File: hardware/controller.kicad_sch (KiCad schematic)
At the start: 2 parts

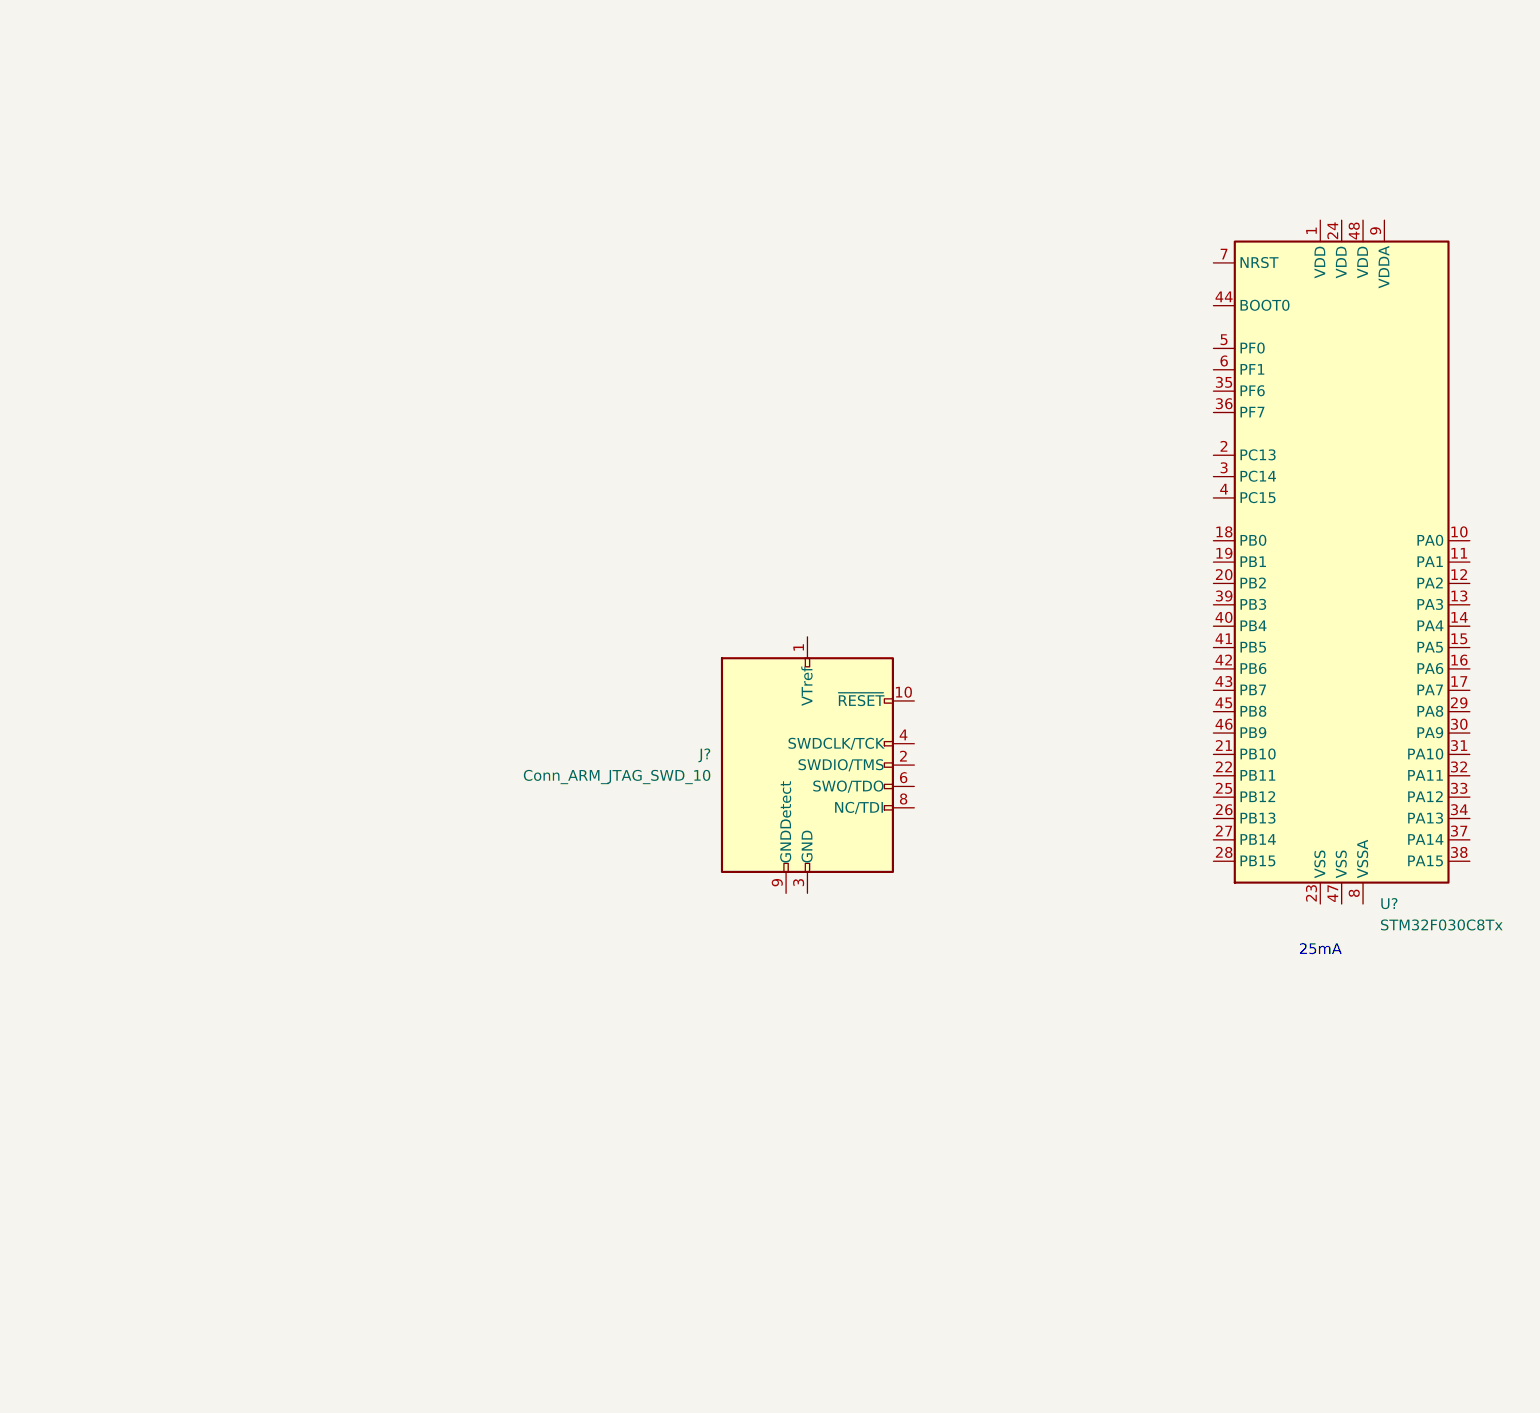
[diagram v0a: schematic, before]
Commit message: MAX5715BAUD lib added
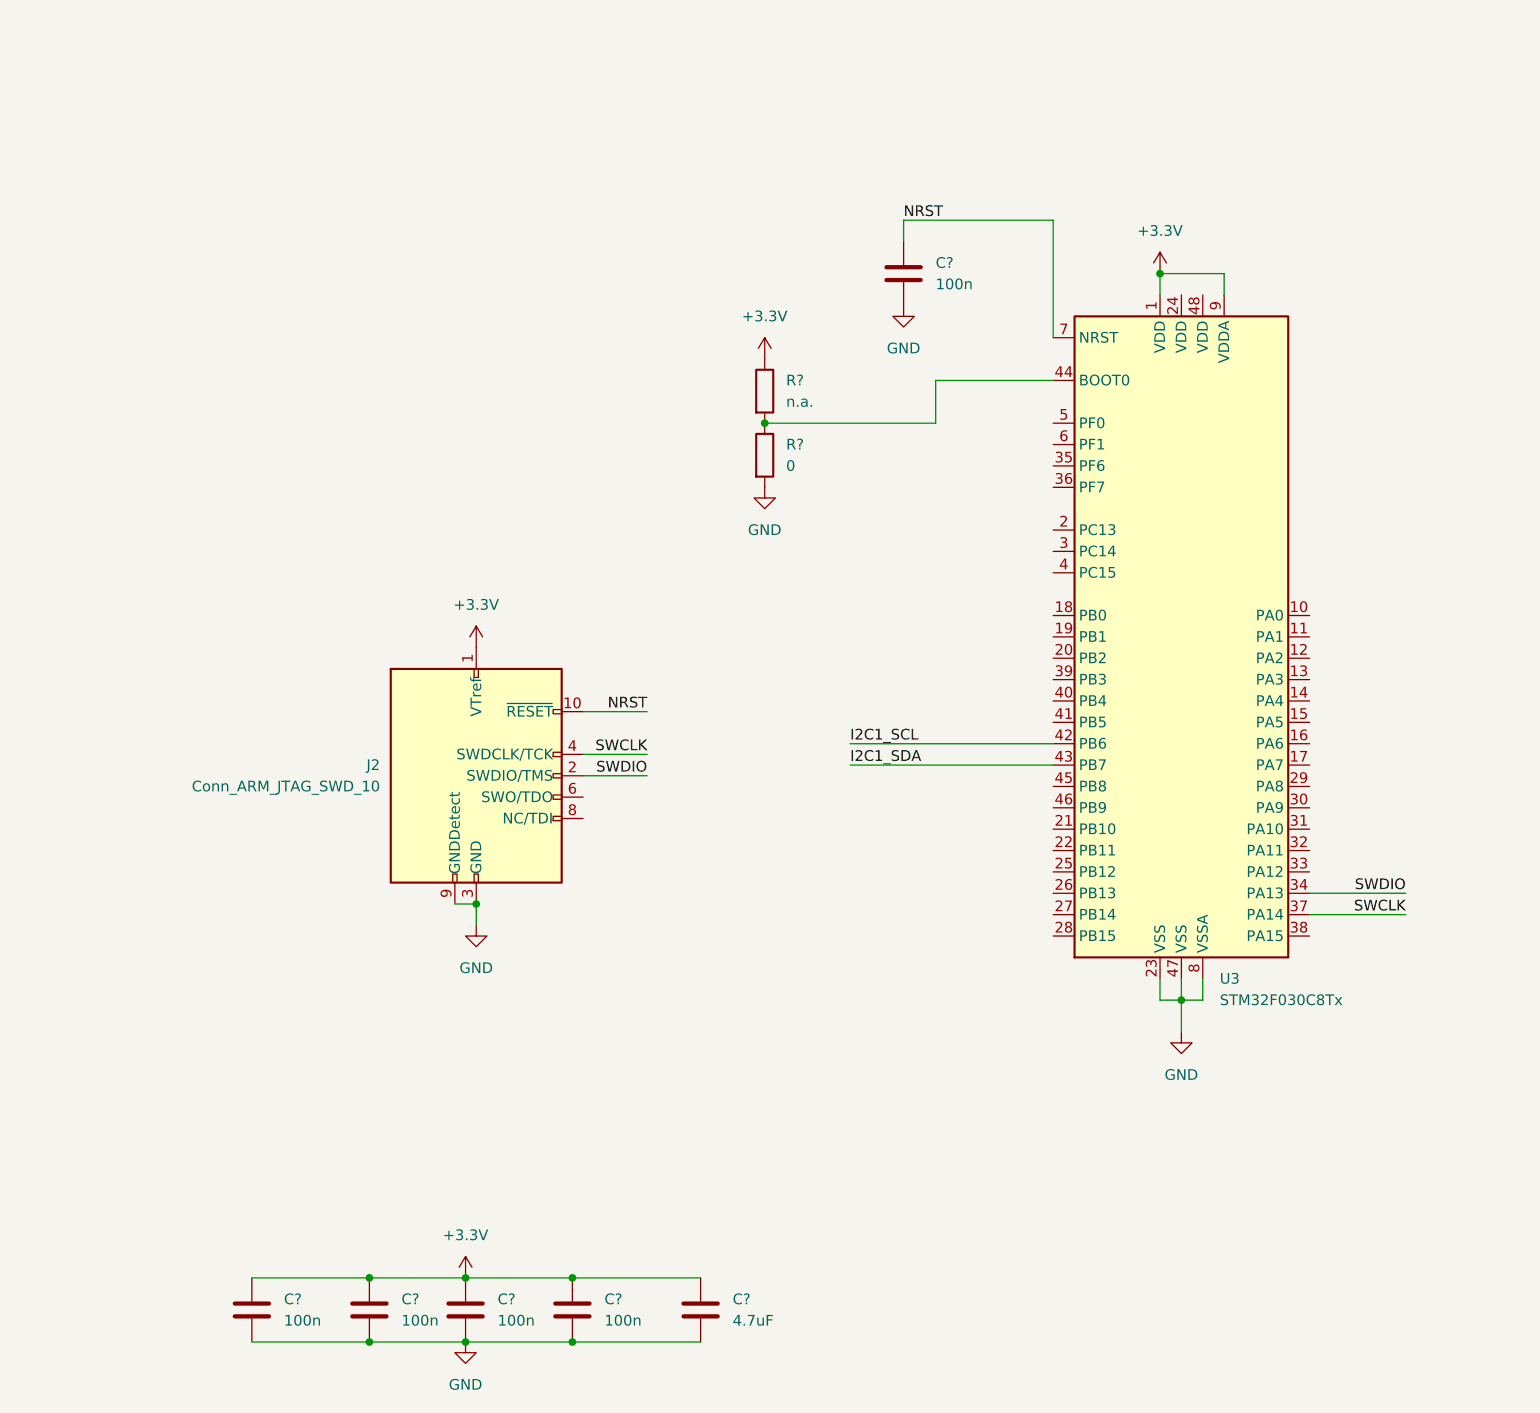
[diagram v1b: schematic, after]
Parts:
- added C? (x5): 100n, Capacitor_SMD:C_0603_1608Metric, symbol Device:C
- added C?: 4.7uF, Capacitor_SMD:C_0805_2012Metric, symbol Device:C
- added R?: 0, Resistor_SMD:R_0603_1608Metric, symbol Device:R
- added R?: n.a., Resistor_SMD:R_0603_1608Metric, symbol Device:R
- gave numbers to parts that had none: 2
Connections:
- net +3V3: now reaches U3.1 (VDD)
- net +3V3: now also J2.1 (VTref), U3.9 (VDDA), C?.1, C?.1, C?.1, C?.1, C?.1, R?.1
- net GND: now reaches U3.23 (VSS)
- net GND: now also J2.3 (GND), J2.5 (GND), J2.9 (GNDDetect), U3.47 (VSS), U3.8 (VSSA), C?.2, C?.2, C?.2, C?.2, C?.2, C?.2, R?.2
- net SWDIO: now reaches U3.34 (PA13)
- net SWDIO: now also J2.2 (SWDIO/TMS)
- net SWCLK: now reaches U3.37 (PA14)
- net SWCLK: now also J2.4 (SWDCLK/TCK)
- net I2C1_SCL: now reaches U3.42 (PB6)
- net I2C1_SDA: now reaches U3.43 (PB7)
- net at U3.44 (BOOT0): now also R?.1, R?.2
- net NRST: now reaches U3.7 (NRST)
- net NRST: now also J2.10 (~{RESET}), C?.1
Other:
- note removed: "25mA"
- moved on the sheet: J2, U3

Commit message: chore: resync local state
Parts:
- added D4: 1N4148WT, Diode_SMD:D_SOD-523, symbol Diode:1N4148WT
- added J3: CUI_SD-50BV, midi_euro_lib:CUI_SD-50BV, symbol midi_euro_lib:CUI_SD-50BV
- added R8: 220, Resistor_SMD:R_0805_2012Metric, symbol Device:R
- added R9: 10k, Resistor_SMD:R_0603_1608Metric, symbol Device:R
- added U6: 6N138, Package_DIP:SMDIP-8_W9.53mm, symbol Isolator:6N138
- gave numbers to parts that had none: 8
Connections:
- net +3V3: now also R9.1, U6.8 (VCC)
- net GND: now also U6.5 (GND)
- new net: D4.1 (K), R8.2, U6.2 (C1)
- new net: D4.2 (A), J3.5, U6.3 (C2)
- new net: J3.4, R8.1
- new net midi_rx: R9.2, U6.6 (VO2)
